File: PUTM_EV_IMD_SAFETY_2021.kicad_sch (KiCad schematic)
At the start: 52 parts, among them J1 MainConn, J2 SafetyConn, K1 FINDER-30.22.7.005.0010, Q1 2N7002, U1 SN74LS32D, U10 74LVC1G79, U11 74LVC1G79, U2 MC78M12CDTG, U3 LM1117IMP-5.0, U4 LM393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

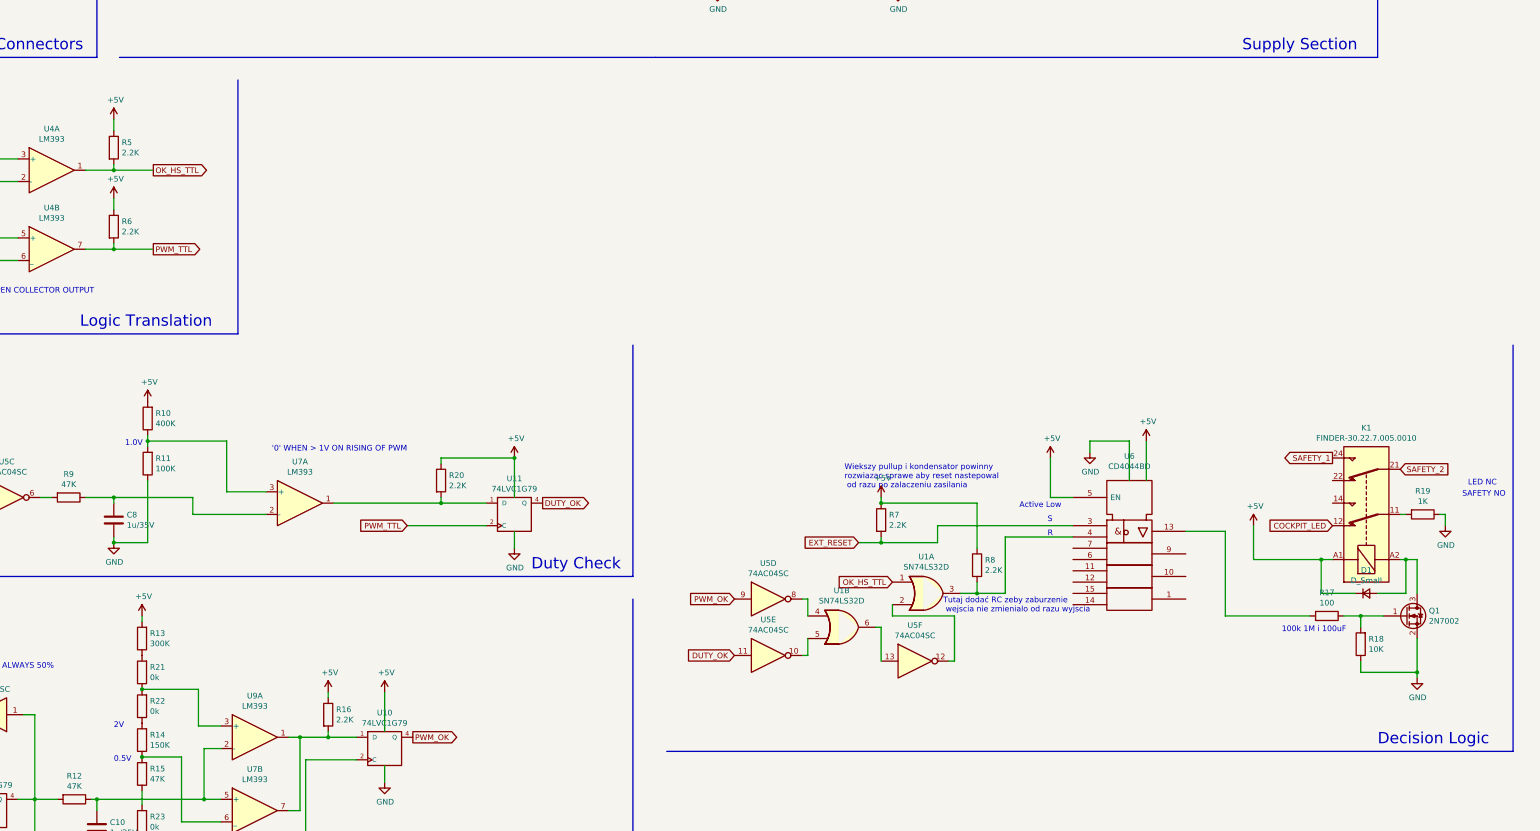
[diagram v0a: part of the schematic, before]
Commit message: Added autoreset into schematic
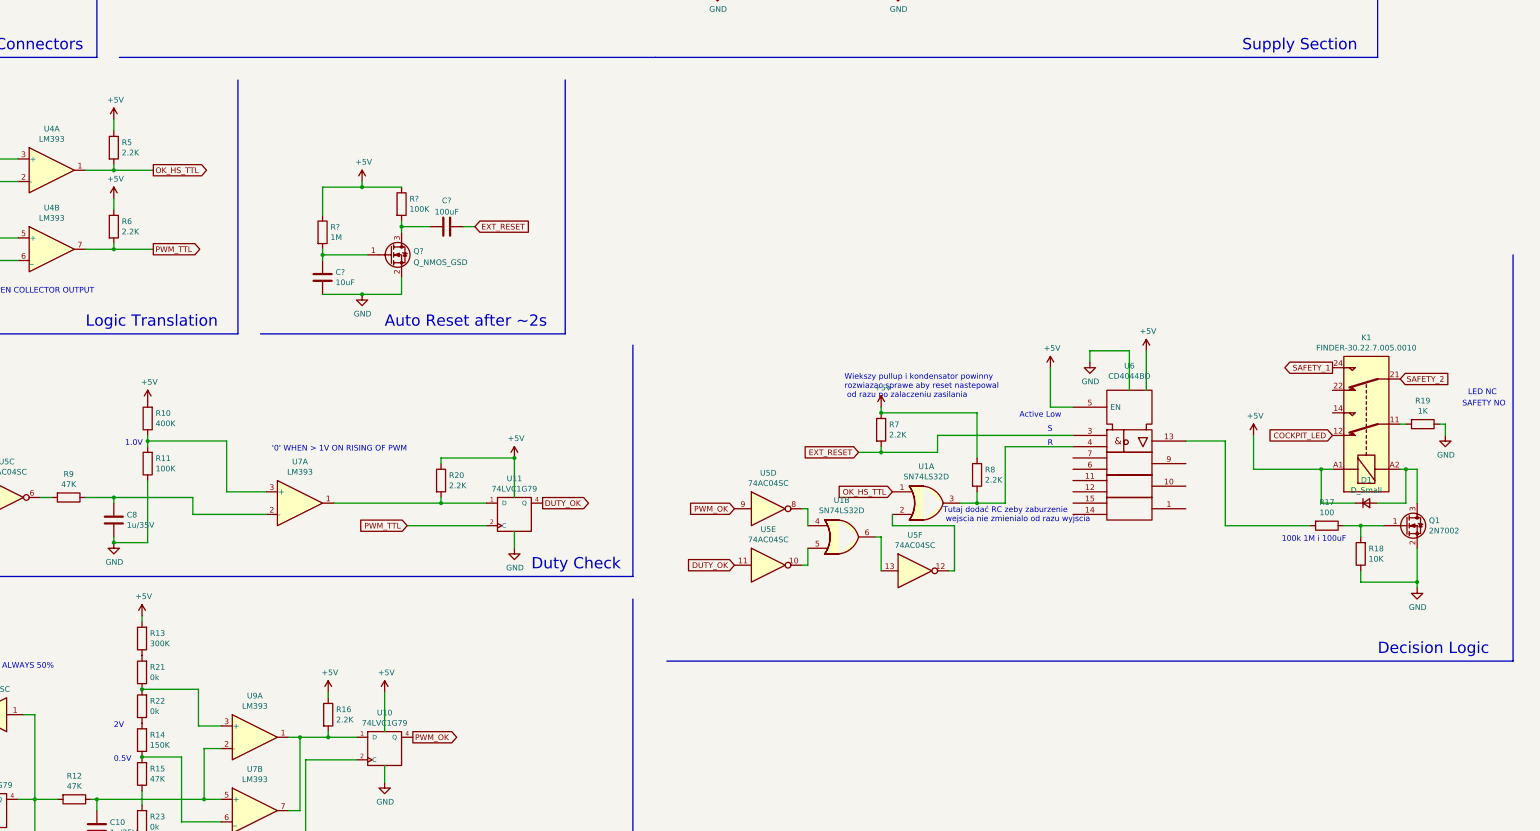
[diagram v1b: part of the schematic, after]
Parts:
- added C?: 10uF, Capacitor_SMD:C_1206_3216Metric, symbol PUTM_EV_IMD_SAFETY_2021-rescue:C-Device
- added C?: 100uF, Capacitor_SMD:C_1206_3216Metric, symbol PUTM_EV_IMD_SAFETY_2021-rescue:C-Device
- added Q?: Q_NMOS_GSD, symbol Device:Q_NMOS_GSD
- added R?: 1M, Resistor_SMD:R_1206_3216Metric, symbol PUTM_EV_IMD_SAFETY_2021-rescue:R-Device
- added R?: 100K, Resistor_SMD:R_1206_3216Metric, symbol PUTM_EV_IMD_SAFETY_2021-rescue:R-Device
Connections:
- net +5V: now also R?.1, R?.1
- net EXT_RESET: now also C?.2
- net GND: now also C?.2, Q?.2 (S)
- new net: C?.1, Q?.1 (G), R?.2
- new net: C?.1, Q?.3 (D), R?.2
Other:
- note added: "Auto Reset after ~2s"
- moved on the sheet: D1, K1, Q1, R17, R18, R19, R7, R8, U1A, U1B, U5D, U5E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

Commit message: Schematic upgraded with hard wired componets
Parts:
- removed U11: 74LVC1G79, Package_TO_SOT_SMD:SOT-23-5, symbol PUTM_EV_IMD_SAFETY_2021-rescue:74LVC1G79-74xGxx
- added C15: 10u, symbol PUTM_EV_IMD_SAFETY_2021-rescue:C-Device
- added C16: 47uF, symbol PUTM_EV_IMD_SAFETY_2021-rescue:C-Device
- added D2, D3: SD103BW, symbol Device:D_Schottky
- added R26: 100K, Resistor_SMD:R_1206_3216Metric, symbol PUTM_EV_IMD_SAFETY_2021-rescue:R-Device
- C13, C14: renamed from C?; footprint Capacitor_SMD:C_1206_3216Metric -> (none)
- Q2: renamed from Q?; value Q_NMOS_GSD -> BSS138W-7-F
- R17: value 100 -> 100k
- R18: value 10K -> 1M
- R7: value 2.2K -> 20K
- gave numbers to parts that had none: 2
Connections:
- net DUTY_OK: now also R20.2, U7.1
- net GND: now also C15.2, C16.2
- net at R17.2, U6.13: now also D3.1 (K)
- net at R8.2, U1.3: now also D2.2 (A), R26.1; no longer U6.4
- net at Q1.1 (G), R17.1, R18.2: now also C16.1, D3.2 (A)
- new net: C15.1, D2.1 (K), R26.2, U6.4
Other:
- note removed: "Tutaj dodać RC zeby zaburzenie wejscia nie zmienialo od razu wyjscia"
- note removed: "Wiekszy pullup i kondensator powinny rozwiazac sprawe aby reset nastepowal od razu po zalaczeniu zasilania"
- moved on the sheet: C13, C14, C8, D1, K1, Q1, Q2, R17, R18, R19, R24, R25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
